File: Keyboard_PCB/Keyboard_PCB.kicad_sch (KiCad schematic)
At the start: 79 parts, among them J1 UART, J3 Conn_ARM_SWD_TagConnect_TC2030, SW1 BOOT, SW2 NRST, U1 S40FC002C1B2I00000, U2 STM32U385VGI6, U3 CC2500, U4 2450BM15B0003001E, Y1 26MHz, Y2 25MHz, Y3 32.786KHz

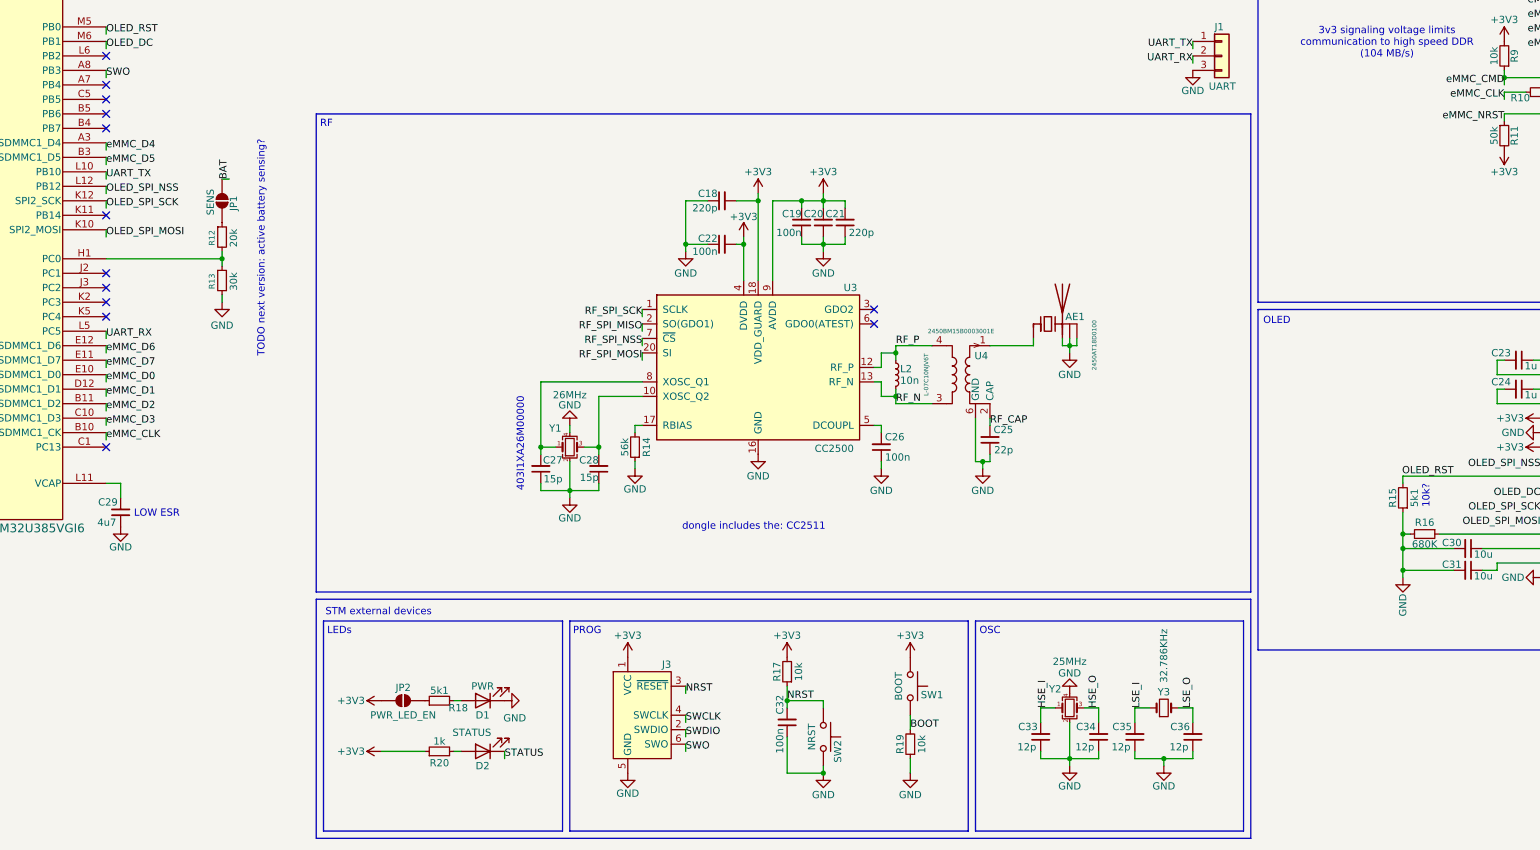
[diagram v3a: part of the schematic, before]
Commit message: Added active battery sensing circuit
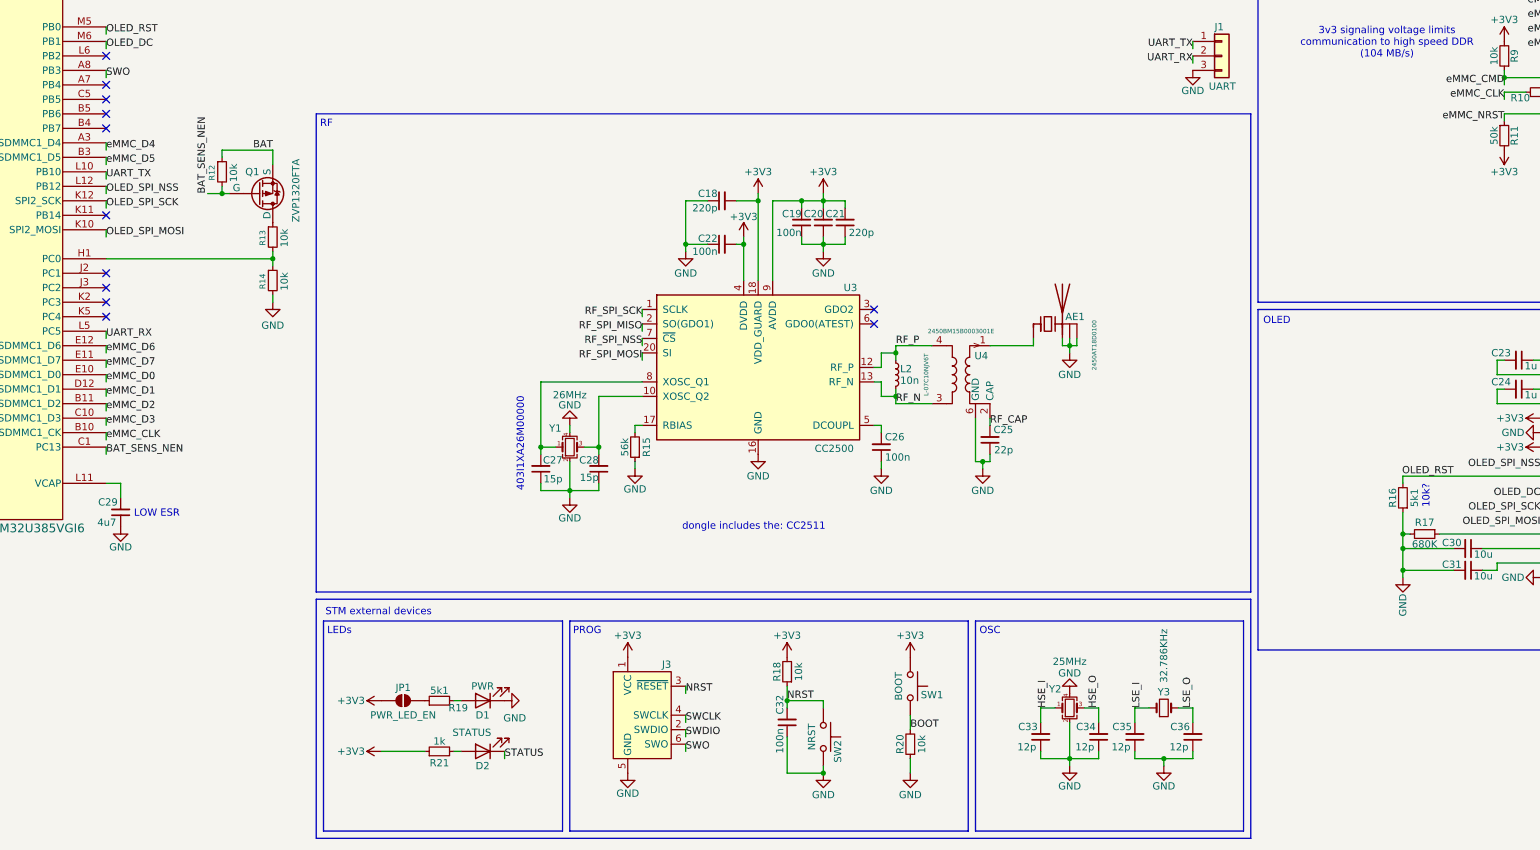
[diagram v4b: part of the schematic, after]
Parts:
- removed JP1: SENS, Jumper:SolderJumper-2_P1.3mm_Open_TrianglePad1.0x1.5mm, symbol Jumper:SolderJumper_2_Open
- added Q1: ZVP1320FTA, Marijn:SOT-323, symbol Simulation_SPICE:PMOS
- added R12: 10k, Resistor_SMD:R_0603_1608Metric, symbol Device:R_Small
- R13: renamed from R12; value 20k -> 10k
- R14: renamed from R13; value 30k -> 10k
- renumbered JP2 to JP1, R14 to R15, R15 to R16, R16 to R17, R17 to R18, R18 to R19, R19 to R20, R20 to R21
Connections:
- net BAT: now also Q1.3 (S), R12.1
- net at R13.1: now also Q1.1 (D)
- net BAT_SENS_NEN: now reaches U2.C1 (PC13)
- net BAT_SENS_NEN: now also Q1.2 (G), R12.2
- no-connect marks 41 -> 40
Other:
- note removed: "TODO next version: active battery sensing?"
- moved on the sheet: R13, R14

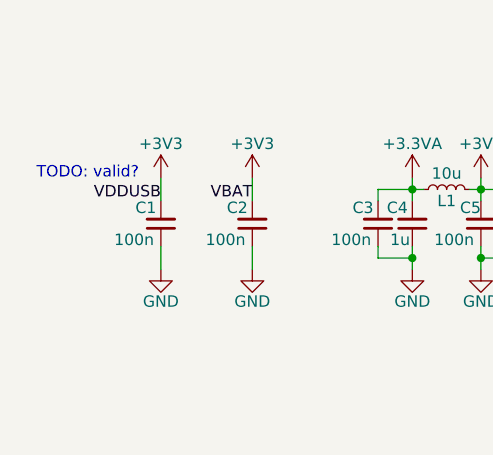
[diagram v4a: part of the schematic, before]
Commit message: Added grid and GND testpoints
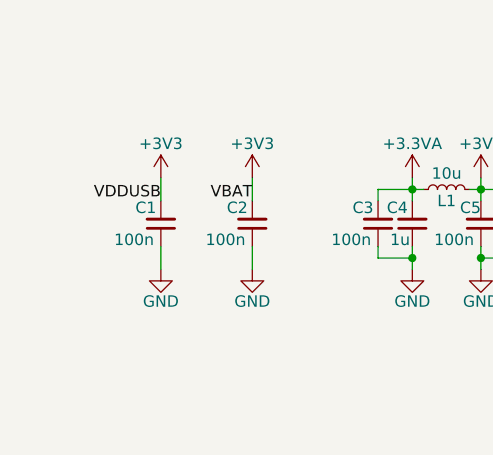
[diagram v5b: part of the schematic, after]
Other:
- note removed: "TODO: valid?"
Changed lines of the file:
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@@
-		)
-	)
-	(text "TODO: valid?"
-		(exclude_from_sim no)
-		(at 35.052 29.972 0)
-		(effects
-			(font
-				(size 1.27 1.27)
-			)
 		)
 	)

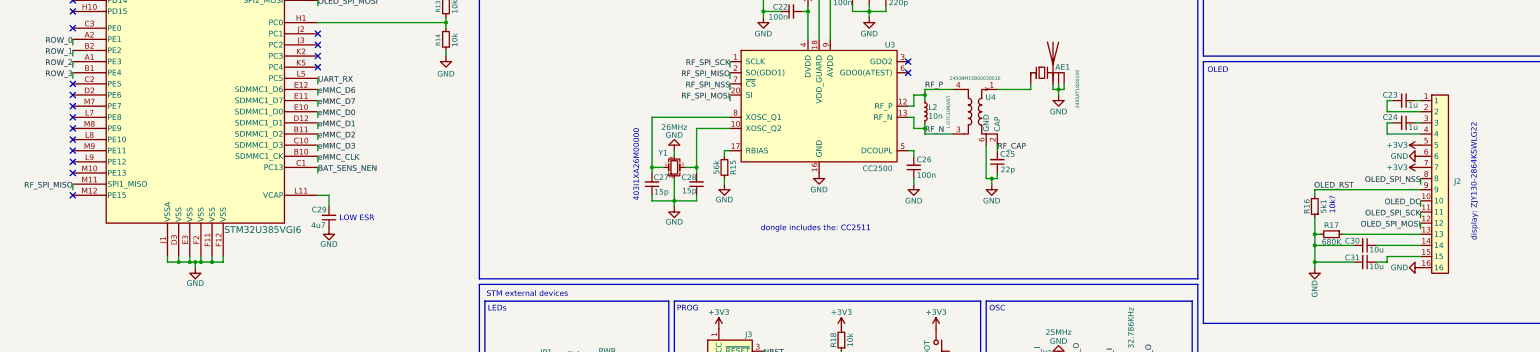
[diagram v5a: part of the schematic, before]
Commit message: Checked and fixed LCD
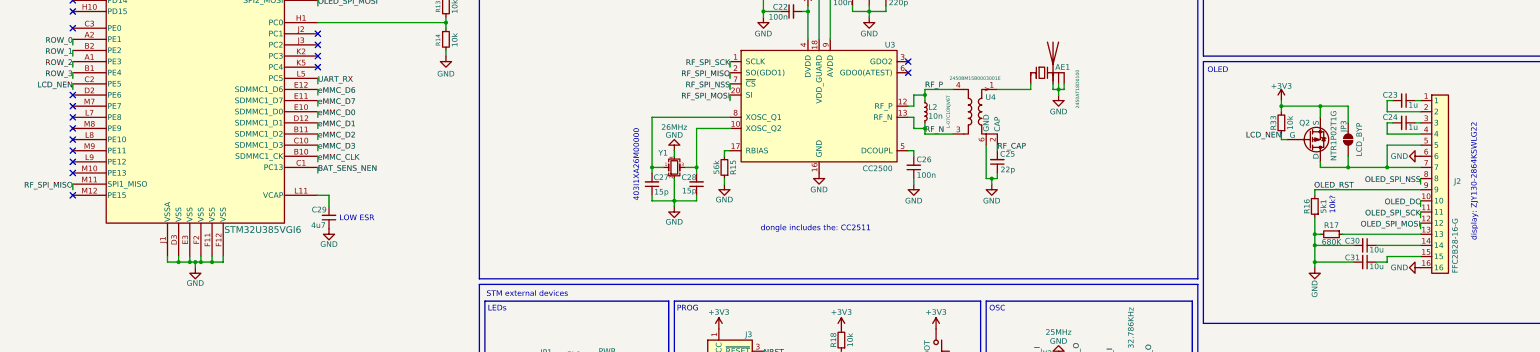
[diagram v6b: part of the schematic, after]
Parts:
- added JP3: LCD_BYP, Jumper:SolderJumper-2_P1.3mm_Open_TrianglePad1.0x1.5mm, symbol Jumper:SolderJumper_2_Open
- added Q2: NTR1P02T1G, Package_TO_SOT_SMD:SOT-23-3, symbol Simulation_SPICE:PMOS
- added R33: 10k, Resistor_SMD:R_0603_1608Metric, symbol Device:R_Small
- J2: value ~ -> FFC2B28-16-G; footprint Marijn:FFC2B28-16-G -> Marijn:FFC2B28-16
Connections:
- net +3V3: now also JP3.2 (B), Q2.3 (S), R33.2; no longer J2.5, J2.7
- net LCD_NEN: now reaches U2.C2 (PE5)
- net LCD_NEN: now also Q2.2 (G), R33.1
- new net: J2.5, J2.7, JP3.1 (A), Q2.1 (D)
- no-connect marks 40 -> 39

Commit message: Dongle and keyboard backup memory
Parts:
- added C45: 100n, Capacitor_SMD:C_0603_1608Metric, symbol Device:C_Small
- added U8: W25Q128JVS, PCM_Package_SO_AKL:SOIC-8_5.23x5.23mm_P1.27mm, symbol Memory_Flash:W25Q128JVS
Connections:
- net +3V3: now also C45.1, U8.8 (VCC)
- net GND: now also C45.2, U8.4 (GND)
- net RF_SPI_MISO: now also U8.5 (DI(IO0))
- net RF_SPI_MOSI: now also U8.2 (DO(IO1))
- net RF_SPI_NSS: now also U8.1 (~{CS})
- net RF_SPI_SCK: now also U8.6 (CLK)
- net BKUP_PMEM_NRST: now reaches U2.M12 (PE15)
- net BKUP_PMEM_NRST: now also U8.7 (IO3)
- net BKUP_PMEM_NWP: now reaches U2.M7 (PE7)
- net BKUP_PMEM_NWP: now also U8.3 (IO2)
- no-connect marks 39 -> 37
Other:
- note added: "ONLY USE INSTEAD OF RF"
- note added: "TODO: never use the small eMMC footprint again without good reason and supply"
- note added: "backup persistent memory"
- moved on the sheet: C1, C10, C2, C3, C4, C5, C6, C7, C8, C9, J1, L1
